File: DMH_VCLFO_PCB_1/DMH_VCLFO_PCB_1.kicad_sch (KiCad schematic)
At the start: 0 parts

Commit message: schematic design in progress
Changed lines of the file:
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@@
 	)
 	(sheet
-		(at 127 88.9)
+		(at 223.52 82.55)
 		(size 20.32 25.4)
 		(exclude_from_sim no)
@@
 		)
 		(property "Sheetname" "Power"
-			(at 127 88.1884 0)
+			(at 223.52 81.8384 0)
 			(effects
 				(font
@@
 		)
 		(property "Sheetfile" "Power.kicad_sch"
-			(at 127 114.8846 0)
+			(at 223.52 108.5346 0)
 			(effects
 				(font
@@
 		)
 		(pin "Bus Gate" output
-			(at 127 96.52 180)
+			(at 223.52 90.17 180)
 			(effects
 				(font
@@
 		)
 		(pin "Bus CV" output
-			(at 127 106.68 180)
+			(at 223.52 100.33 180)
 			(effects
 				(font
@@
 		)
 		(instances
-			(project "DMH-Kosmo-10cm-PCB"
+			(project "DMH_VCLFO_PCB_1"
 				(path "/58f4306d-5387-4983-bb08-41a2313fd315"
 					(page "4")
@@
 	)
 	(sheet
-		(at 63.5 76.2)
+		(at 63.5 38.1)
 		(size 50.8 50.8)
 		(exclude_from_sim no)
@@
 		)
 		(property "Sheetname" "Core Circuit"
-			(at 63.5 75.4884 0)
+			(at 63.5 37.3884 0)
 			(effects
 				(font
@@
 		)
 		(property "Sheetfile" "Core_Circuit.kicad_sch"
-			(at 63.5 127.5846 0)
+			(at 63.5 89.4846 0)
 			(effects
 				(font
@@
 		)
 		(instances
-			(project "DMH-Kosmo-10cm-PCB"
+			(project "DMH_VCLFO_PCB_1"
 				(path "/58f4306d-5387-4983-bb08-41a2313fd315"
 					(page "3")
@@
 	)
 	(sheet
-		(at 25.4 76.2)
+		(at 25.4 38.1)
 		(size 25.4 50.8)
 		(exclude_from_sim no)
@@
 		)
 		(property "Sheetname" "Inputs and Outputs"
-			(at 25.4 75.4884 0)
+			(at 25.4 37.3884 0)
 			(effects
 				(font
@@
 		)
 		(property "Sheetfile" "Inputs_and_Outputs.kicad_sch"
-			(at 25.4 127.5846 0)
+			(at 25.4 89.4846 0)
 			(effects
 				(font
@@
 		)
 		(instances
-			(project "DMH-Kosmo-10cm-PCB"
+			(project "DMH_VCLFO_PCB_1"
 				(path "/58f4306d-5387-4983-bb08-41a2313fd315"
 					(page "2")

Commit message: Ready for breadboarding
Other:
- sheet Core Circuit renamed Core Circuit A
- sheet Inputs and Outputs renamed Inputs and Outputs A
- sheet Core Circuit A ports: added CV In, Pot In, Rmp, Rnd, Rng_Sw_1, Rng_Sw_2, Saw, Sin, Sqr, Sync In, Tri; removed none
- sheet Inputs and Outputs A ports: added CV A, Pot A, Rmp, Rnd, Rng_Sw_1, Rng_Sw_2, Saw, Sin, Sqr, Sync A, Tri; removed none
- sheet Power ports: added none; removed Bus CV, Bus Gate

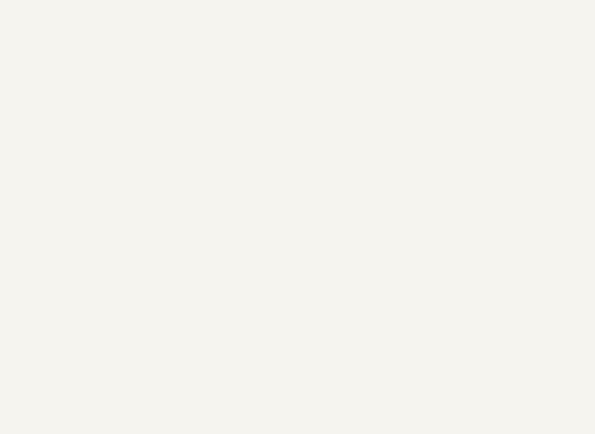
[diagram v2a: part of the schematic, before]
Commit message: Documented breadboard layout
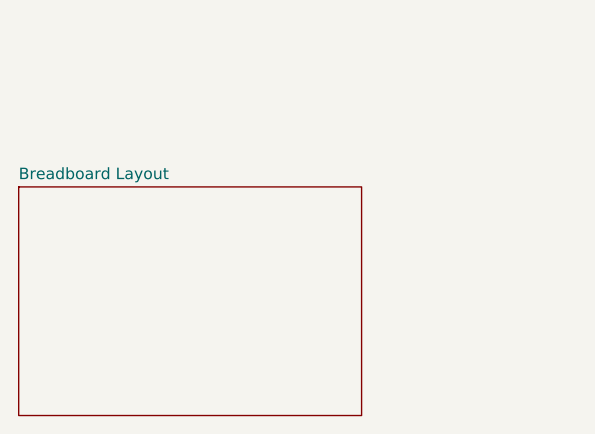
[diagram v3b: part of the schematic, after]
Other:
- added sheet Breadboard Layout (Breadboard_Layout.kicad_sch)
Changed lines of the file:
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@@
+	)
+	(sheet
+		(at 25.4 165.1)
+		(size 38.1 25.4)
+		(exclude_from_sim no)
+		(in_bom yes)
+		(on_board yes)
+		(dnp no)
+		(fields_autoplaced yes)
+		(stroke
+			(width 0.1524)
+			(type solid)
+		)
+		(fill
+			(color 0 0 0 0.0000)
+		)
+		(property "Sheetname" "Breadboard Layout"
+			(at 25.4 164.3884 0)
+			(effects
+				(font
+					(size 1.27 1.27)
+				)
+				(justify left bottom)
+			)
+		)
+		(property "Sheetfile" "Breadboard_Layout.kicad_sch"
+			(at 25.4 191.0846 0)
+			(effects
+				(font
+					(size 1.27 1.27)
+				)
+				(justify left top)
+				(hide yes)
+			)
+		)
+		(instances
+			(project "DMH_VCLFO_PCB_1"
+				(path "/58f4306d-5387-4983-bb08-41a2313fd315"
+					(page "5")
+				)
+			)
+		)
 	)
 	(sheet

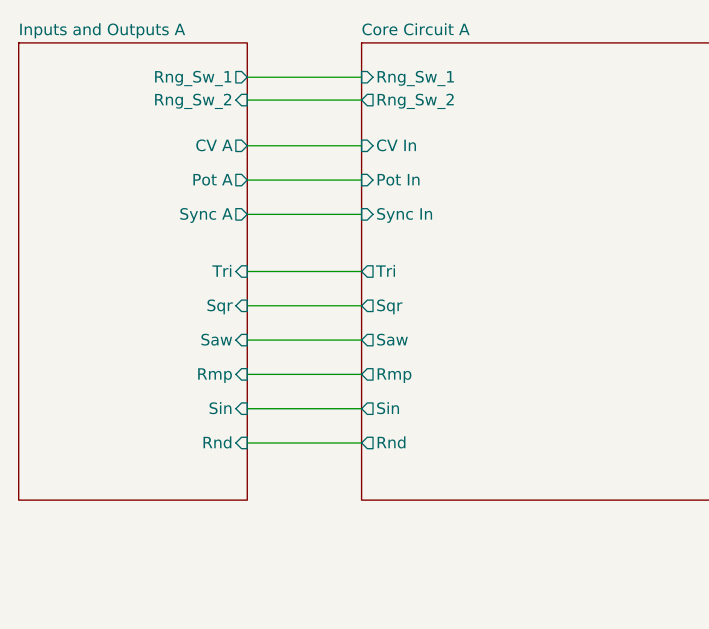
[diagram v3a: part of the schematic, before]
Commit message: Added super fast range option
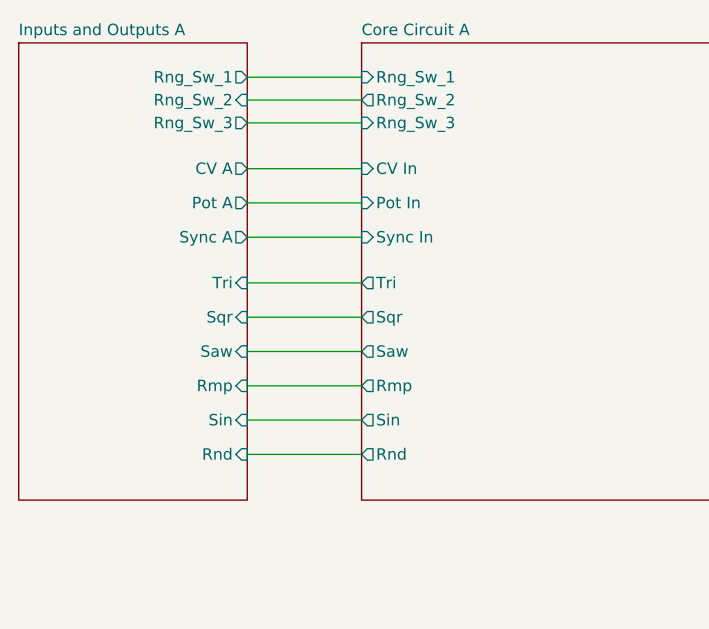
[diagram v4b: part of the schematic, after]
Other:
- sheet Core Circuit A ports: added Rng_Sw_3; removed none
- sheet Inputs and Outputs A ports: added Rng_Sw_3; removed none
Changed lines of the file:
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@@
 	(wire
 		(pts
-			(xy 50.8 63.5) (xy 63.5 63.5)
+			(xy 50.8 66.04) (xy 63.5 66.04)
 		)
 		(stroke
@@
 	(wire
 		(pts
-			(xy 50.8 81.28) (xy 63.5 81.28)
-		)
-		(stroke
-			(width 0)
-			(type default)
-		)
-	)
-	(wire
-		(pts
-			(xy 50.8 85.09) (xy 63.5 85.09)
-		)
-		(stroke
-			(width 0)
-			(type default)
-		)
-	)
-	(wire
-		(pts
-			(xy 50.8 55.88) (xy 63.5 55.88)
+			(xy 50.8 82.55) (xy 63.5 82.55)
+		)
+		(stroke
+			(width 0)
+			(type default)
+		)
+	)
+	(wire
+		(pts
+			(xy 50.8 86.36) (xy 63.5 86.36)
+		)
+		(stroke
+			(width 0)
+			(type default)
+		)
+	)
+	(wire
+		(pts
+			(xy 50.8 58.42) (xy 63.5 58.42)
 		)
 		(stroke
@@
 	(wire
 		(pts
-			(xy 50.8 69.85) (xy 63.5 69.85)
-		)
-		(stroke
-			(width 0)
-			(type default)
-		)
-	)
-	(wire
-		(pts
-			(xy 50.8 59.69) (xy 63.5 59.69)
-		)
-		(stroke
-			(width 0)
-			(type default)
-		)
-	)
-	(wire
-		(pts
-			(xy 50.8 77.47) (xy 63.5 77.47)
-		)
-		(stroke
-			(width 0)
-			(type default)
-		)
-	)
-	(wire
-		(pts
-			(xy 50.8 88.9) (xy 63.5 88.9)
-		)
-		(stroke
-			(width 0)
-			(type default)
-		)
-	)
-	(wire
-		(pts
-			(xy 50.8 73.66) (xy 63.5 73.66)
+			(xy 50.8 71.12) (xy 63.5 71.12)
+		)
+		(stroke
+			(width 0)
+			(type default)
+		)
+	)
+	(wire
+		(pts
+			(xy 50.8 62.23) (xy 63.5 62.23)
+		)
+		(stroke
+			(width 0)
+			(type default)
+		)
+	)
+	(wire
+		(pts
+			(xy 50.8 78.74) (xy 63.5 78.74)
+		)
+		(stroke
+			(width 0)
+			(type default)
+		)
+	)
+	(wire
+		(pts
+			(xy 50.8 90.17) (xy 63.5 90.17)
+		)
+		(stroke
+			(width 0)
+			(type default)
+		)
+	)
+	(wire
+		(pts
+			(xy 50.8 74.93) (xy 63.5 74.93)
+		)
+		(stroke
+			(width 0)
+			(type default)
+		)
+	)
+	(wire
+		(pts
+			(xy 50.8 53.34) (xy 63.5 53.34)
 		)
 		(stroke
@@
 		)
 		(pin "Rmp" output
-			(at 63.5 81.28 180)
+			(at 63.5 82.55 180)
 			(effects
 				(font
@@
 		)
 		(pin "Rnd" output
-			(at 63.5 88.9 180)
+			(at 63.5 90.17 180)
 			(effects
 				(font
@@
 		)
 		(pin "Saw" output
-			(at 63.5 77.47 180)
+			(at 63.5 78.74 180)
 			(effects
 				(font
@@
 		)
 		(pin "Sin" output
-			(at 63.5 85.09 180)
+			(at 63.5 86.36 180)
 			(effects
 				(font
@@
 		)
 		(pin "Sqr" output
-			(at 63.5 73.66 180)
+			(at 63.5 74.93 180)
 			(effects
 				(font
@@
 		)
 		(pin "Tri" output
-			(at 63.5 69.85 180)
+			(at 63.5 71.12 180)
 			(effects
 				(font
@@
 		)
 		(pin "CV In" input
-			(at 63.5 55.88 180)
+			(at 63.5 58.42 180)
 			(effects
 				(font
@@
 		)
 		(pin "Pot In" input
-			(at 63.5 59.69 180)
+			(at 63.5 62.23 180)
 			(effects
 				(font
@@
 		)
 		(pin "Sync In" input
-			(at 63.5 63.5 180)
+			(at 63.5 66.04 180)
 			(effects
 				(font
@@
 		(pin "Rng_Sw_2" output
 			(at 63.5 50.8 180)
+			(effects
+				(font
+					(size 1.27 1.27)
+				)
+				(justify left)
+			)
+		)
+		(pin "Rng_Sw_3" input
+			(at 63.5 53.34 180)
 			(effects
 				(font
@@
 		)
 		(pin "Rmp" input
-			(at 50.8 81.28 0)
+			(at 50.8 82.55 0)
 			(effects
 				(font
@@
 		)
 		(pin "Rnd" input
-			(at 50.8 88.9 0)
+			(at 50.8 90.17 0)
 			(effects
 				(font
@@
 		)
 		(pin "Saw" input
-			(at 50.8 77.47 0)
+			(at 50.8 78.74 0)
 			(effects
 				(font
@@
 		)
 		(pin "Sin" input
-			(at 50.8 85.09 0)
+			(at 50.8 86.36 0)
 			(effects
 				(font
@@
 		)
 		(pin "Sqr" input
-			(at 50.8 73.66 0)
+			(at 50.8 74.93 0)
 			(effects
 				(font
@@
 		)
 		(pin "Tri" input
-			(at 50.8 69.85 0)
+			(at 50.8 71.12 0)
 			(effects
 				(font
@@
 		)
 		(pin "CV A" output
-			(at 50.8 55.88 0)
+			(at 50.8 58.42 0)
 			(effects
 				(font
@@
 		)
 		(pin "Pot A" output
-			(at 50.8 59.69 0)
+			(at 50.8 62.23 0)
 			(effects
 				(font
@@
 		)
 		(pin "Sync A" output
-			(at 50.8 63.5 0)
+			(at 50.8 66.04 0)
 			(effects
 				(font
@@
 			(effects
 				(font
+					(size 1.27 1.27)
+				)
+				(justify right)
+			)
+		)
+		(pin "Rng_Sw_3" output
+			(at 50.8 53.34 0)
+			(effects
+				(font
